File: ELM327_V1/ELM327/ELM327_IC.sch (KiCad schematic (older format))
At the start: 37 parts

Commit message: update to elm327 done missing esp32 missing GPS missing GSM
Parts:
- removed C?: CP1, symbol Device:CP1
- removed C?: 0.1uF, symbol Device:CP1
- removed C?: 0.1uF 50V, symbol Device:CP1
- added C? (x2): 0.1uF, symbol Device:C
- added C?: 1uF, symbol Device:C
- added C? (x3): 0.1uF, symbol Device:CP
- added D? (x2): 1N4148, Diode_THT:D_DO-35_SOD27_P7.62mm_Horizontal, symbol Diode:1N4148
- added D?: LED, symbol Device:LED
- added Q? (x2): 2N3906, Package_TO_SOT_THT:TO-92_Inline, symbol Transistor_BJT:2N3906
- added Q? (x3): 2N3904, Package_TO_SOT_THT:TO-92_Inline, symbol Transistor_BJT:2N3904
- added R? (x4): 10K, symbol Device:R
- added R? (x4): 4.7K, symbol Device:R
- added R? (x2): 470, symbol Device:R
- added R? (x2): 2.2K, symbol Device:R
- added R? (x2): 22K, symbol Device:R
- added R?: 47K, symbol Device:R
- added R?: 100K, symbol Device:R
- added R? (x2): 560, symbol Device:R
- added R?: 330, symbol Device:R
- added U? (x2): LM317L_SOT-89, Package_TO_SOT_SMD:SOT-89-3, symbol Regulator_Linear:LM317L_SOT-89
- added U?: TXB0102DCT, Package_SO:TSSOP-8_3x3mm_P0.65mm, symbol Logic_LevelTranslator:TXB0102DCT
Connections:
- net +12V: now also C?.1, R?.1, U?.3 (VI), U?.3 (VI)
- net +5V: now also C?.1, C?.2, R?.2, U?.7 (VCCB)
- net ELM327_02: now also C?.1
- net ELM327_03: now also R?.2
- net ELM327_04: now also R?.1
- net ELM327_11: now also R?.1, R?.2
- net ELM327_13: now also Q?.3 (C), R?.1
- net ELM327_14: now also R?.1
- net ELM327_17: now also U?.1 (B2)
- net ELM327_18: now also U?.8 (B1)
- net GND: now also C?.1, C?.2, C?.2, C?.2, C?.2, C?.2, D?.1 (K), Q?.1 (E), Q?.1 (E), Q?.1 (E), R?.1, R?.1, R?.2, R?.2, R?.2, U?.2 (GND)
- net J1850-Bus+: now also D?.1 (K), R?.1, R?.2, R?.2
- net J1850-Bus-: now also D?.1 (K), Q?.1 (E), Q?.3 (C), R?.1, R?.2, R?.2
- new net: D?.2 (A), Q?.3 (C)
- new net: Q?.1 (E), R?.1, R?.1, U?.2 (VO)
- new net: Q?.2 (B), R?.2, R?.2
- new net: Q?.3 (C), R?.1
- new net: Q?.2 (B), R?.2 (x2)
- new net: R?.2, R?.2, U?.1 (ADJ)
- new net: R?.1, R?.1, R?.2
- new net: D?.2 (A), Q?.2 (B), R?.1
- new net: Q?.2 (B), Q?.3 (C), R?.1
- new net: R?.1, R?.2, U?.1 (ADJ)
- new net: D?.2 (A), R?.2
- new net +3V3: C?.1, C?.1, R?.1, U?.2 (VO), U?.3 (VCCA)
- new net ELM327_RX: U?.4 (A2)
- new net ELM327_TX: U?.5 (A1)
- new net ENABLE_PIN_LEVELSHIFTER: R?.1, U?.6 (OE)
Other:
- note added: "3.3V regulator"
- note added: "ELM327_LEVEL_SHIFTER_IN/OUT/ENABLE"
- note added: "J1850-Bus +/-"

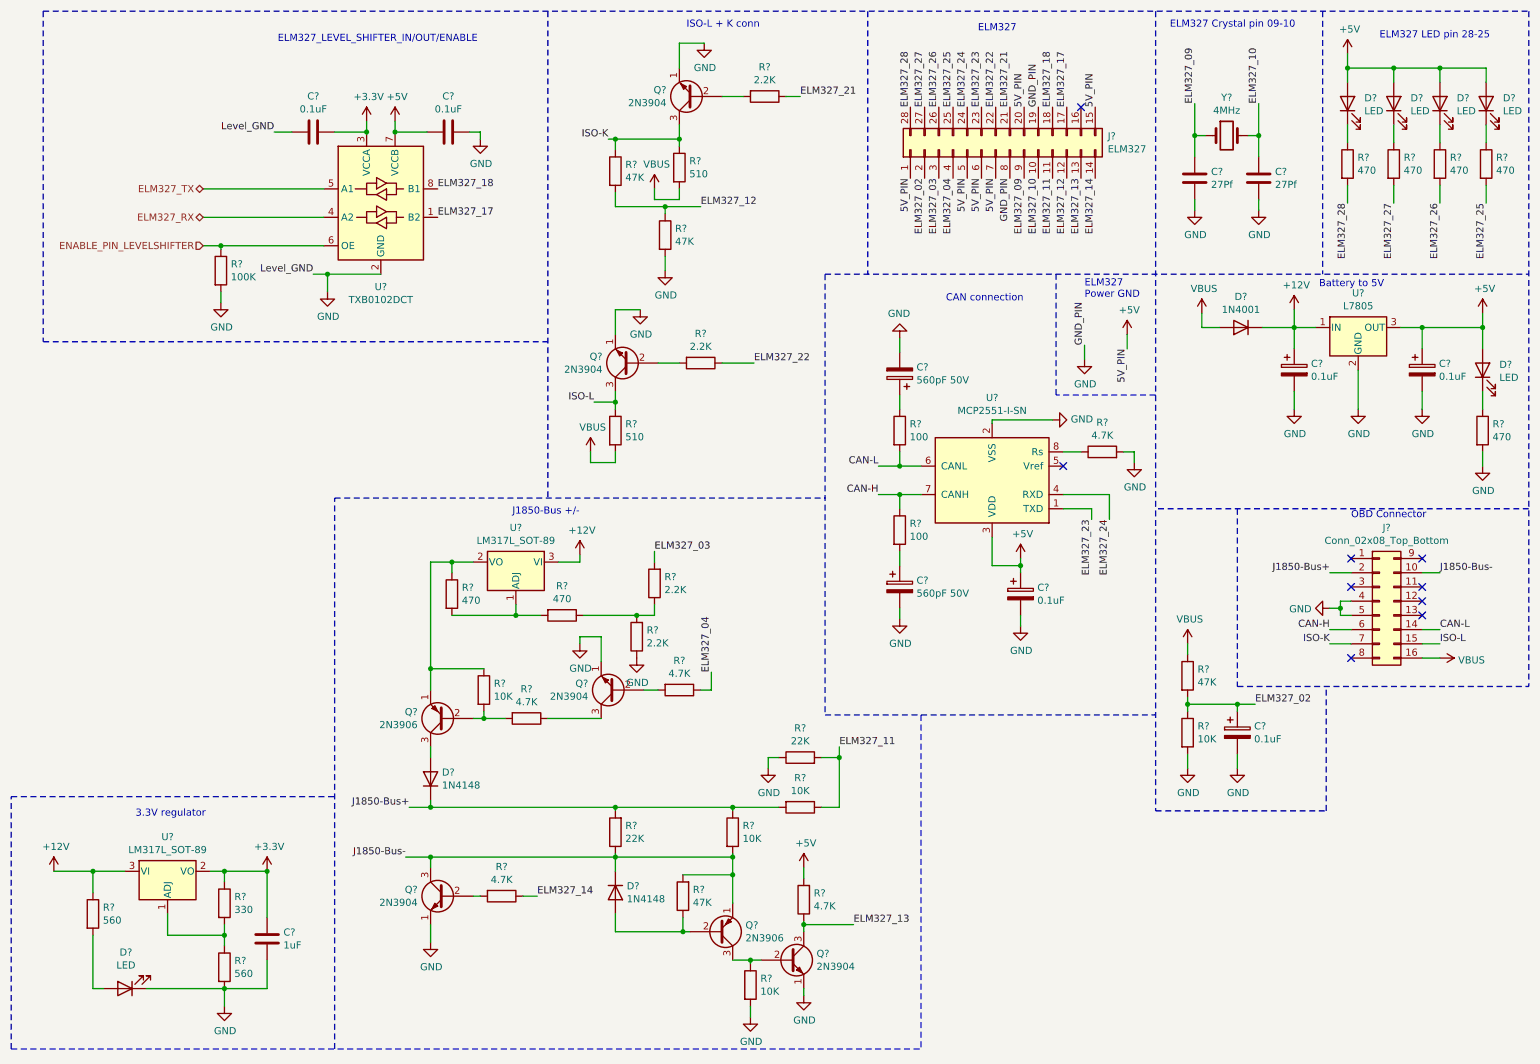
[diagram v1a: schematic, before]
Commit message: update to elm327 and data sheet
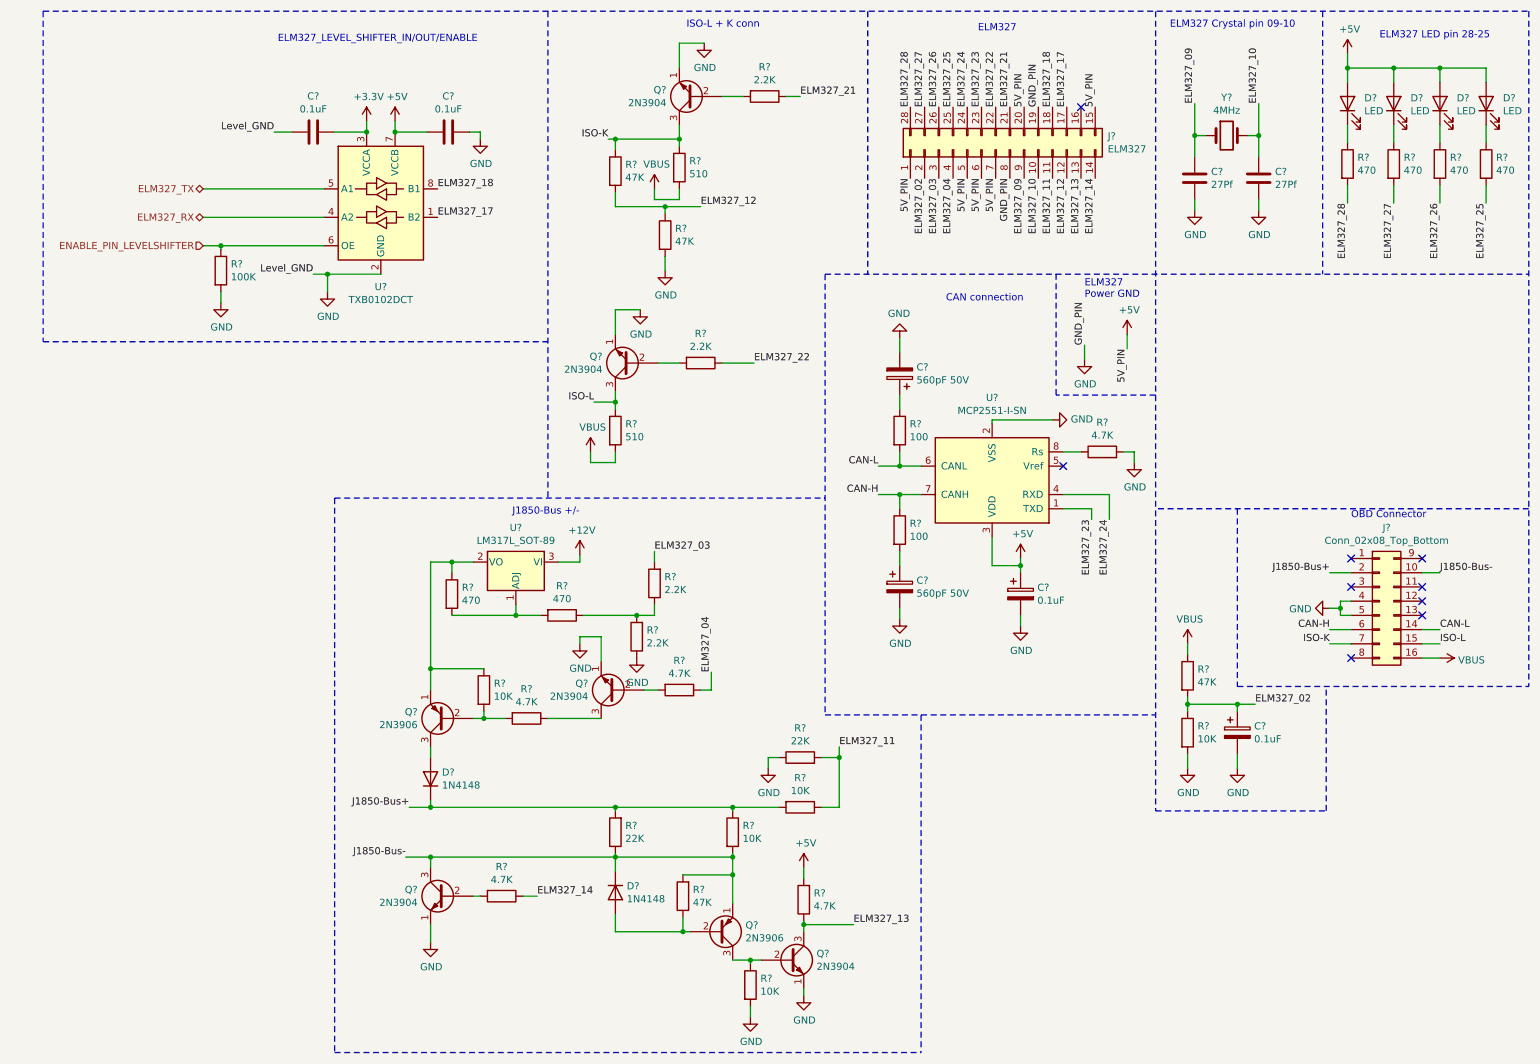
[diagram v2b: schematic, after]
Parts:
- removed C?: 1uF, symbol Device:C
- removed C? (x2): 0.1uF, symbol Device:CP
- removed D? (x2): LED, symbol Device:LED
- removed D?: 1N4001, symbol Simulation_SPICE:DIODE
- removed R?: 470, symbol Device:R
- removed R? (x2): 560, symbol Device:R
- removed R?: 330, symbol Device:R
- removed U?: L7805, symbol Regulator_Linear:L7805
- removed U?: LM317L_SOT-89, Package_TO_SOT_SMD:SOT-89-3, symbol Regulator_Linear:LM317L_SOT-89
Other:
- note removed: "3.3V regulator"
- note removed: "Battery to 5V"
